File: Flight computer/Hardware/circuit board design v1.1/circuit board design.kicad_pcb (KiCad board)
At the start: 4 copper layers, 30.5 x 82.6 mm, 83 parts, among them J1 Conn_01x05, J2 USB_B_Micro, J3 Screw_Terminal_01x04, J4 Conn_01x02, J6 Conn_Coaxial, J7 Conn_Coaxial, U1 LSM9DS1, U11 W25Q64JVSSIM, U14 MAX40200AUK, U15 LD3985M33R_TSOT23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

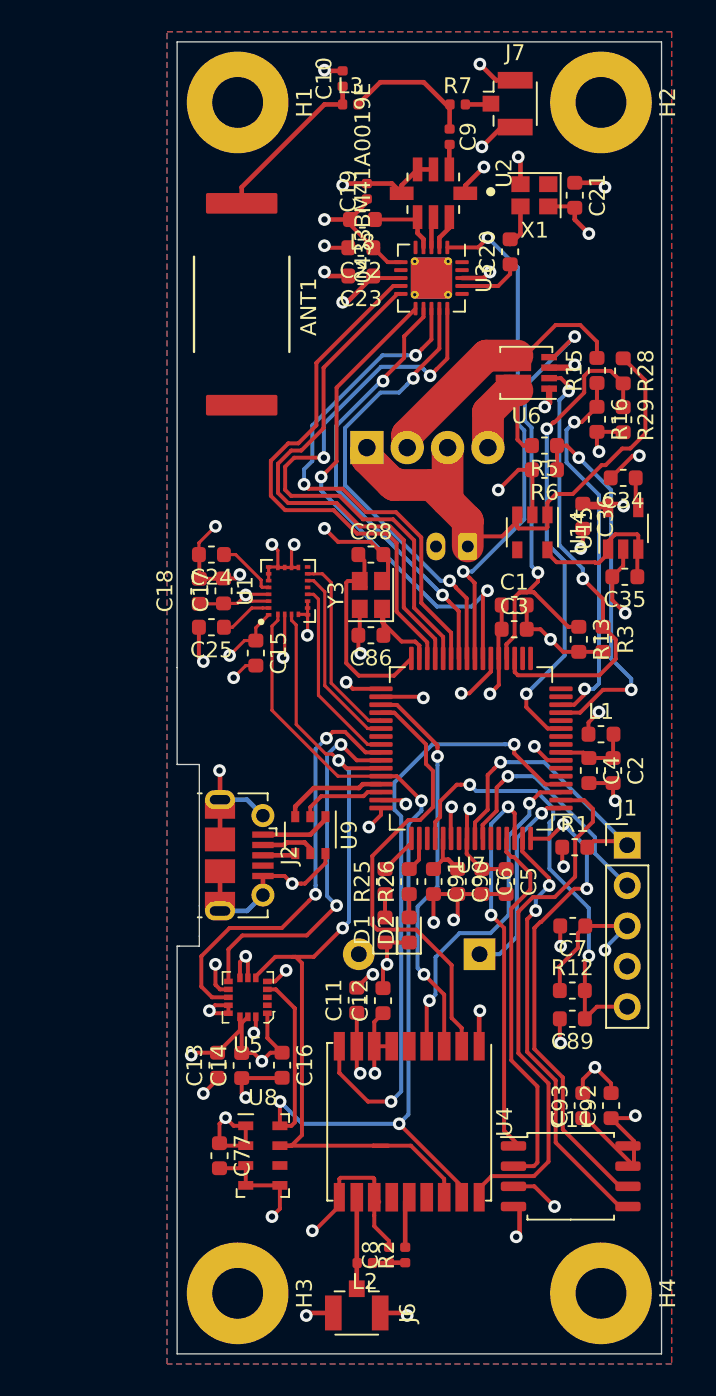
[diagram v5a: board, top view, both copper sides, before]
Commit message: changed GPS to M8Q and included the diode from V bus to foot print which I missed out
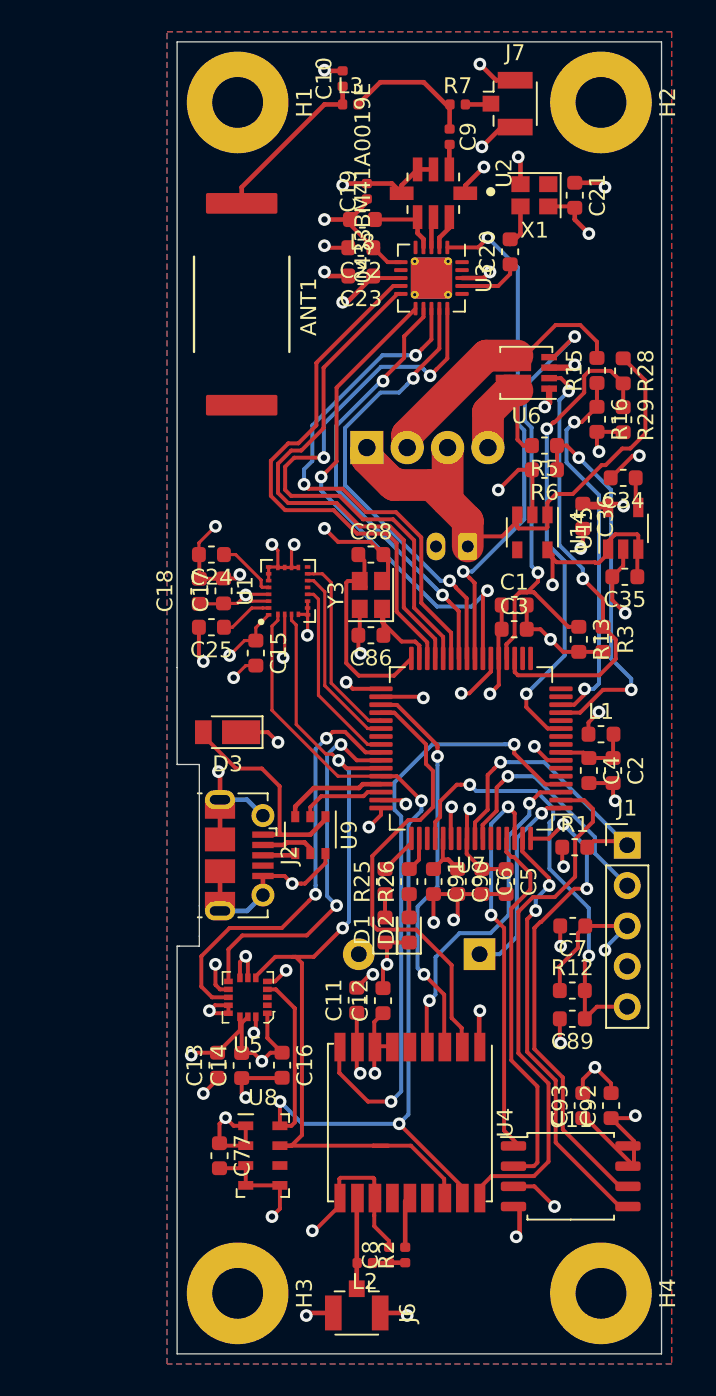
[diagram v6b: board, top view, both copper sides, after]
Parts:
- removed G***: LOGO, flight-computer:ICSS_Logo
- added D3: DFLS130L, Diode_SMD:D_PowerDI-123, F.Cu at (95.5, 101.2)
- C19: value 270pf -> 270pF
- R1, R12, R25, R26: value 1K -> 1.6K
- R15, R28, R29, R5: value 100K -> 120K
- U4: value MAX-M8C -> MAX-M8Q
- moved U4 0.07 mm to (107.0, 125.8)
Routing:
- net Net-(C35-Pad1): track 10.0 -> 36.4 mm, vias 0 -> 2
- net VBUS: track 4.98 -> 15.3 mm

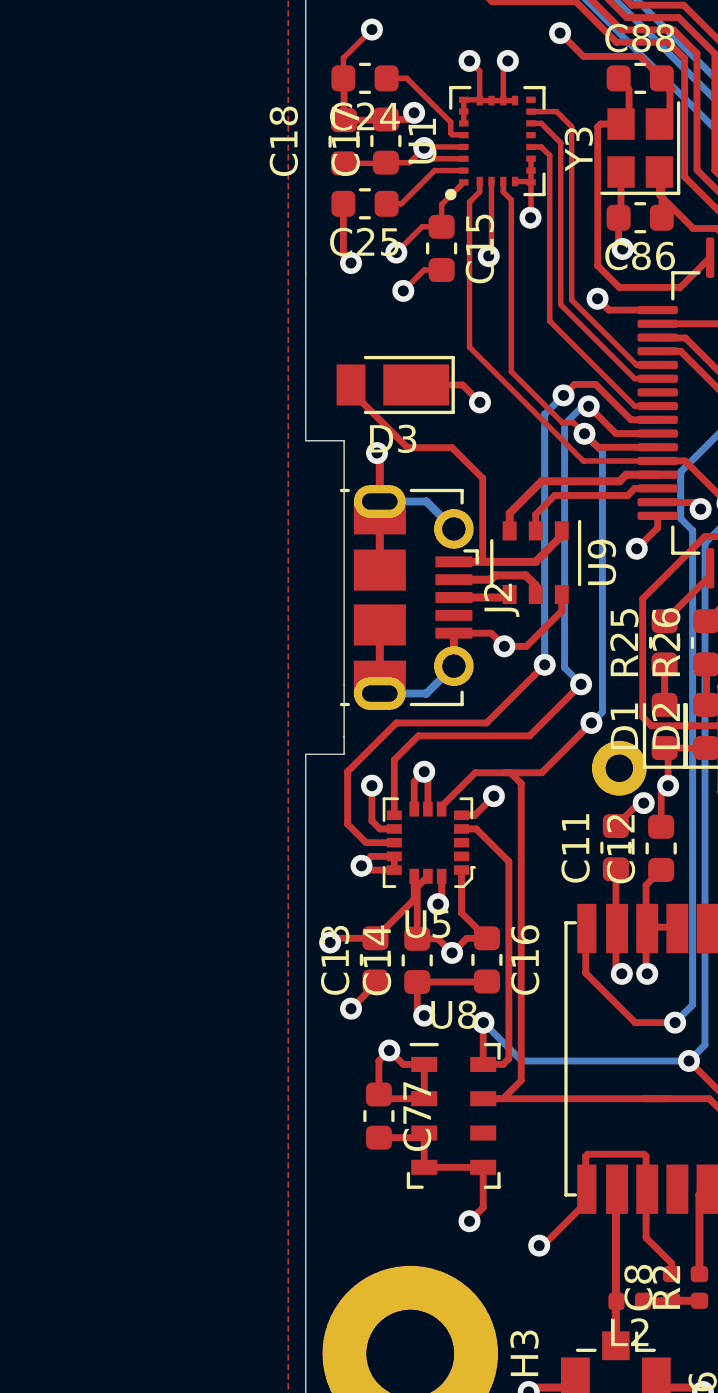
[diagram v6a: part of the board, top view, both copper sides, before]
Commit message: added in grove connector for break out pins. Made a new software framework for SAMD
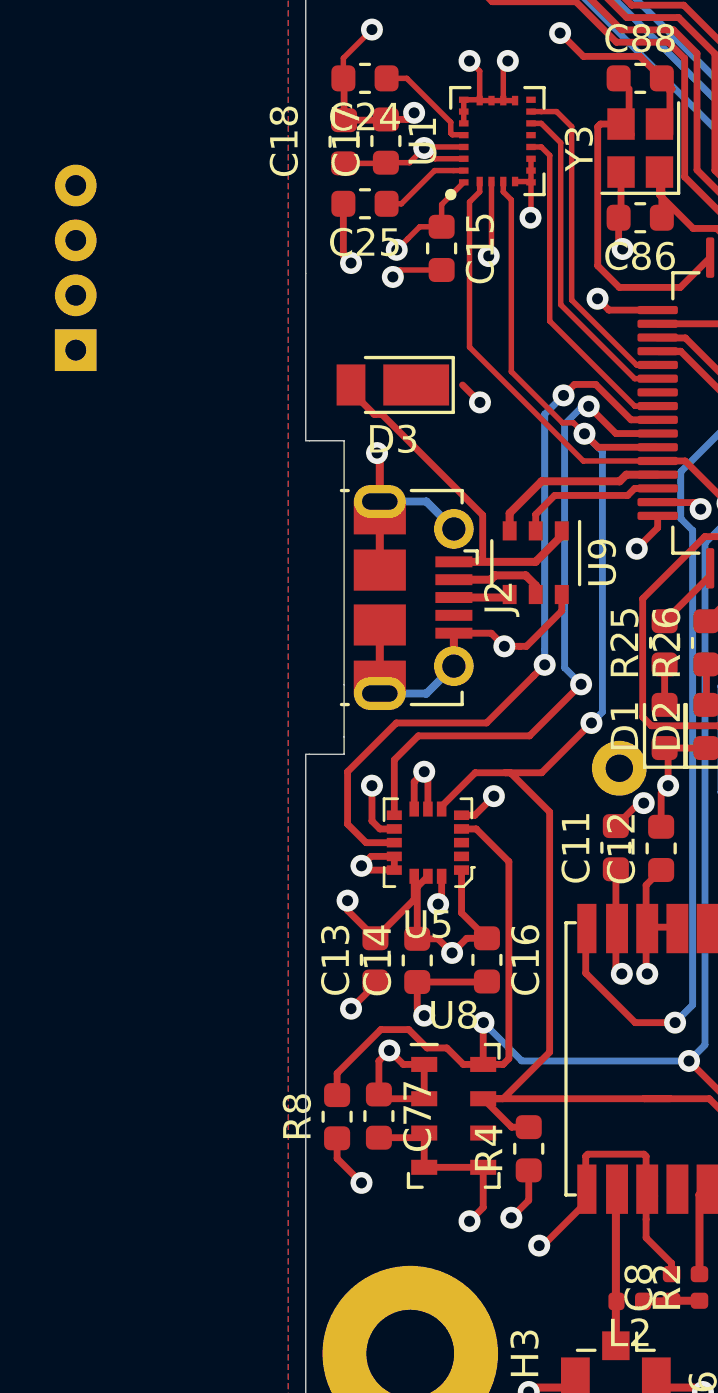
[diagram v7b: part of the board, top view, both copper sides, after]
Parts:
- added J5: Conn_01x04, flight-computer:NS-Tech_Grove_1x04_P2mm_Vertical, B.Cu at (83.9, 99.9)
- added R4: 4.7K, Resistor_SMD:R_0603_1608Metric, F.Cu at (100.5, 129.1)
- added R8: 4.7K, Resistor_SMD:R_0603_1608Metric, F.Cu at (93.5, 127.9)
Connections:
- U7 pad 17: Net-(U7-Pad17) -> /MCU/SDA_PA08
- U7 pad 18: Net-(U7-Pad18) -> /MCU/SCL_PA09
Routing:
- net /gps/GPS_SCL: track 65.5 -> 72.8 mm
- net +3V3: track 109.5 -> 113.5 mm, vias 23 -> 25
- net /gps/GPS_SDA: track 57.8 -> 60.8 mm
- net Net-(C35-Pad1): track 36.4 -> 34.7 mm
- net VBUS: track 15.3 -> 14.6 mm

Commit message: almost done
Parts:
- added G***: LOGO, flight-computer:ICSS_Logo, B.Cu at (107.4, 101.1)
- moved J5 43.7 mm to (119.5, 74.5)
- moved C21 3.47 mm to (115.7, 70.5), turned to 90 degrees
- moved R13 2.26 mm to (115.8, 94.0)
- moved R3 2.26 mm to (117.3, 94.0)
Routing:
- net /MCU/SDA_PA08: track 0.00 -> 43.8 mm, vias 0 -> 1
- net /MCU/SCL_PA09: track 0.00 -> 39.7 mm, vias 0 -> 1
- net /pyro_driver/FIRE_A: track 28.7 -> 32.6 mm
- net /pyro_driver/FIRE_B: track 29.8 -> 32.4 mm
- net Net-(C35-Pad1): track 34.7 -> 36.7 mm
- net GND: track 172.6 -> 170.7 mm
- net +3V3: track 113.5 -> 115.3 mm
- net /MCU/MCU_PA05: track 24.9 -> 26.4 mm
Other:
- net class sense added: clearance 0.2, trace_width 0.25, via_dia 0.8, via_drill 0.4
- board text added: "Rocket Flight Computer v1.1 Imperial College Space Society Medad Newman, Richard Ibbotson 2019"
- board text removed: "Rocket Flight Computer v1.0 Imperial College Space Society Medad Newman, Richard Ibbotson Sept 2019"
